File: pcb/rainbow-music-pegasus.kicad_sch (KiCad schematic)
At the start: 83 parts, among them J1 USB_B_Micro, J2 Conn_02x03_Odd_Even, SW1 SW_SPDT, U1 ESP32-C3-MINI-1, U2 OPA344NA, U3 TLV75533PDBV

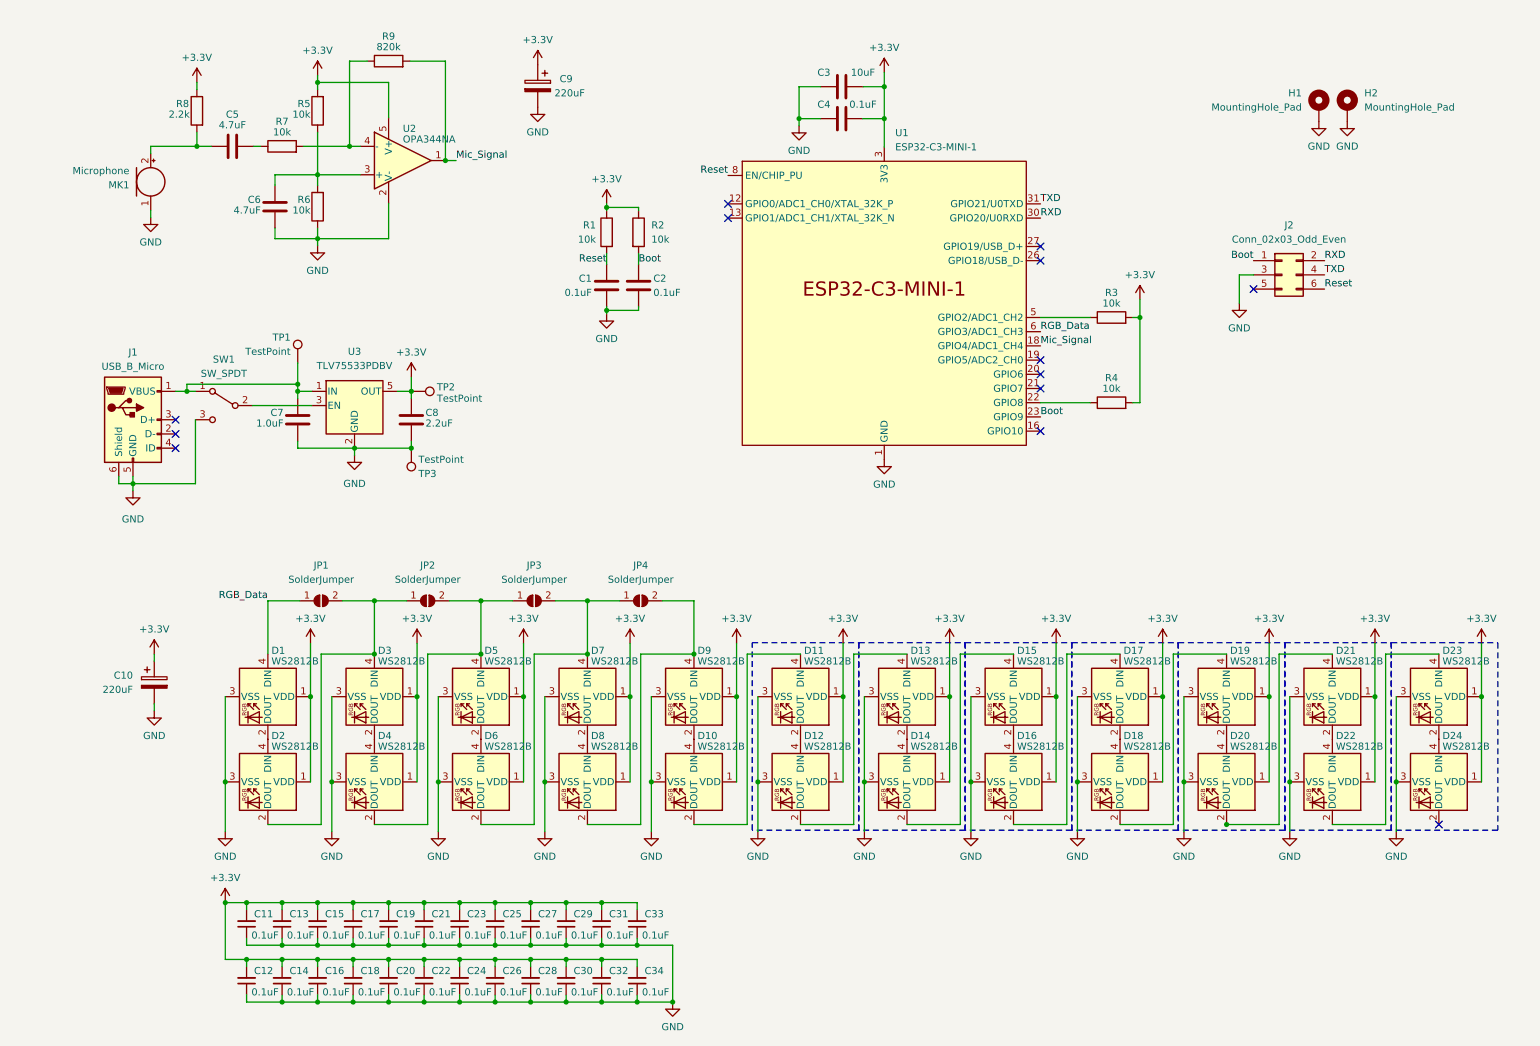
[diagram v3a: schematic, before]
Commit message: Added Altivo cartoon to silkscreen, jumpers for configuring total LEDs installed
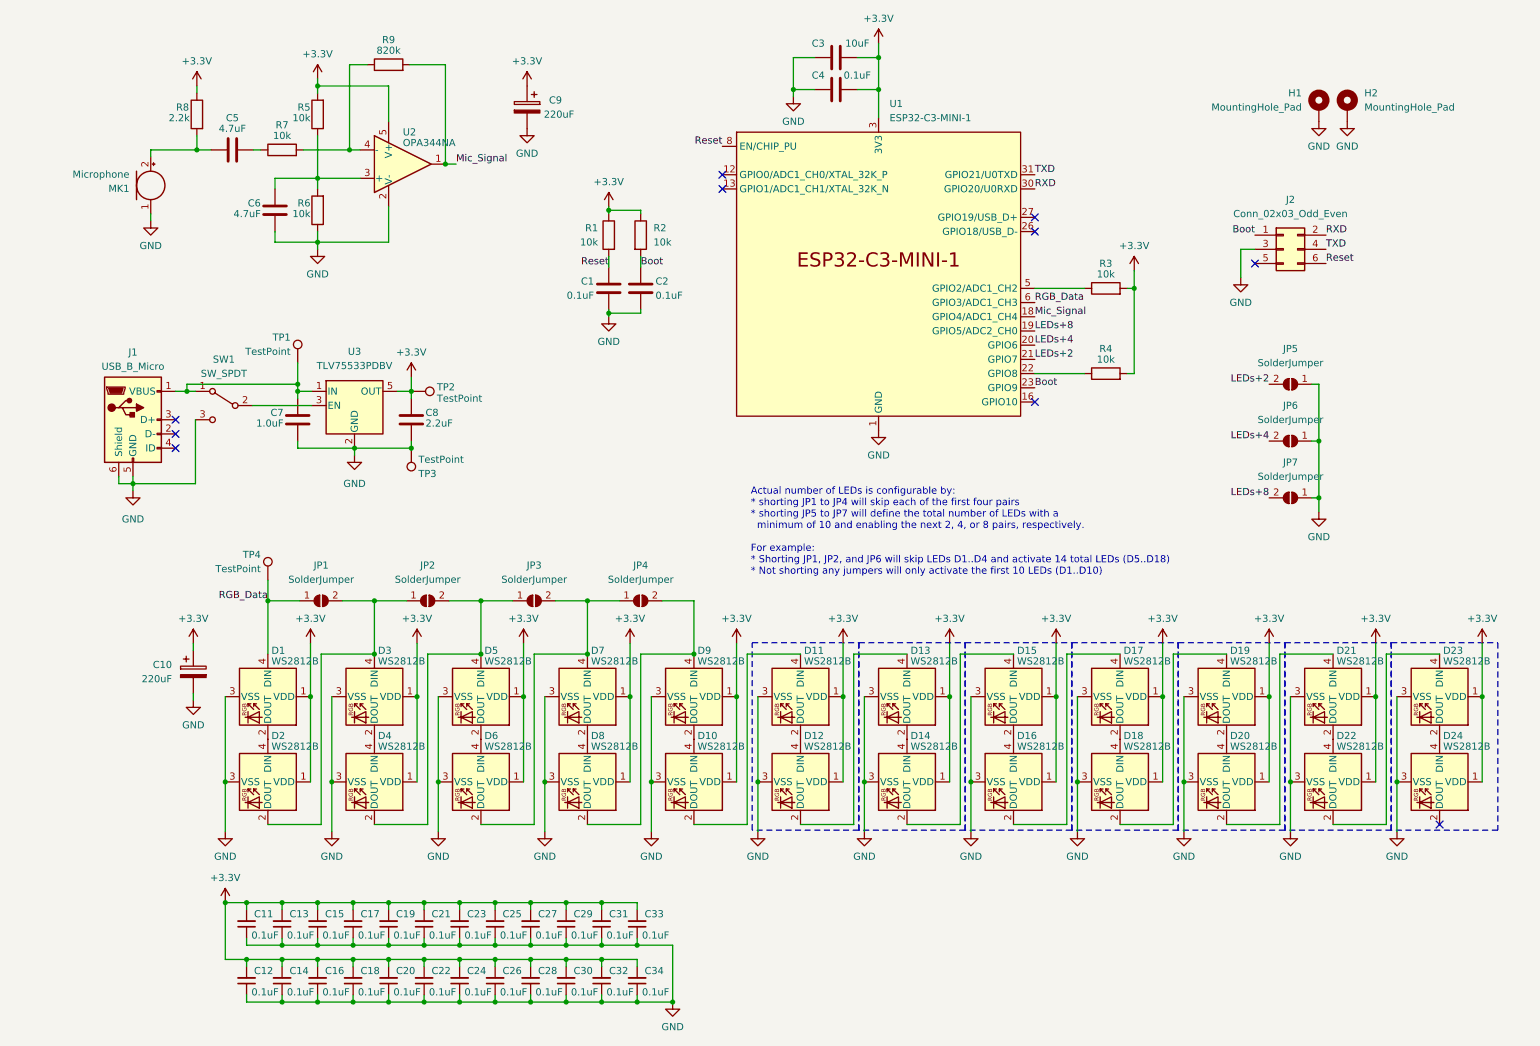
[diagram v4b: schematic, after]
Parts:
- added JP5, JP6, JP7: SolderJumper, Jumper:SolderJumper-2_P1.3mm_Open_TrianglePad1.0x1.5mm, symbol Jumper:SolderJumper_2_Open
- added TP4: TestPoint, TestPoint:TestPoint_THTPad_1.5x1.5mm_Drill0.7mm, symbol Connector:TestPoint
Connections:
- net GND: now also JP5.1 (A), JP6.1 (A), JP7.1 (A)
- net RGB_Data: now also TP4.1
- net LEDs+8: now reaches U1.19 (GPIO5/ADC2_CH0)
- net LEDs+8: now also JP7.2 (B)
- net LEDs+4: now reaches U1.20 (GPIO6)
- net LEDs+4: now also JP6.2 (B)
- net LEDs+2: now reaches U1.21 (GPIO7)
- net LEDs+2: now also JP5.2 (B)
- no-connect marks 13 -> 10
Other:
- note added: "Actual number of LEDs is configurable by: * shorting JP1 to JP4 will skip each of the first four pairs * shorting JP5 to JP7 will define the total number of LEDs with a minimum of 10 and enabling the next 2, 4, or 8 pairs, respectively. For example: * Shorting JP1, JP2, and JP6 will skip LEDs D1..D4 and activate 14 total LEDs (D5..D18) * Not shorting any jumpers will only activate the first 10 LE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"
- moved on the sheet: C1, C10, C2, C3, C4, C5, C6, C9, J2, MK1, R1, R2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

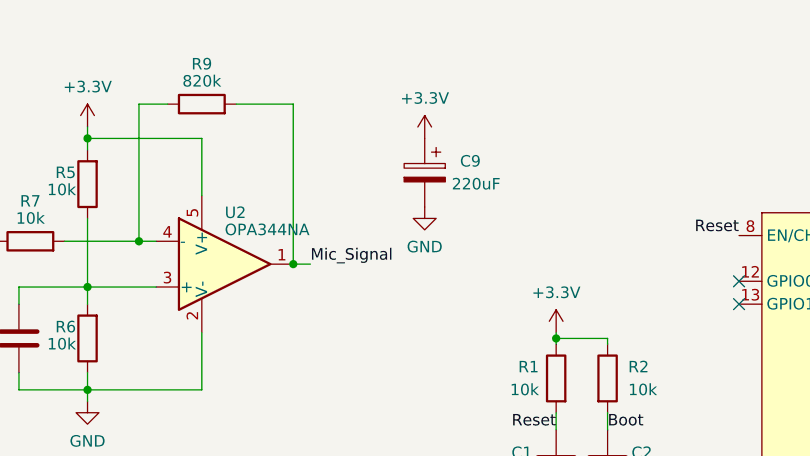
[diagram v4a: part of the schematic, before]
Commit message: Missed a decoupling capacitor at U2; added as C35
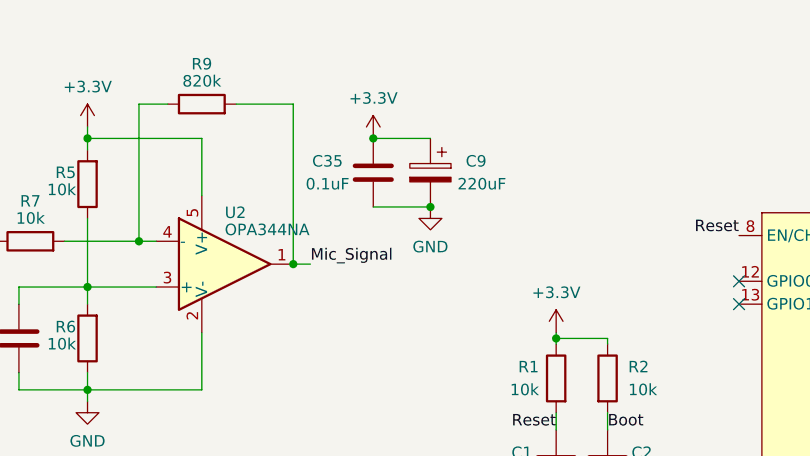
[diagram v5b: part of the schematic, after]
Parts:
- added C35: 0.1uF, Capacitor_SMD:C_0603_1608Metric, symbol Device:C
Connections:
- net +3.3V: now also C35.2
- net GND: now also C35.1
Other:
- moved on the sheet: C9
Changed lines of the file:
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@@
   (junction (at 119.38 180.34) (diameter 0) (color 0 0 0 0)
   )
+  (junction (at 106.68 34.29) (diameter 0) (color 0 0 0 0)
+  )
   (junction (at 74.93 190.5) (diameter 0) (color 0 0 0 0)
   )
@@
   (junction (at 97.79 118.745) (diameter 0) (color 0 0 0 0)
   )
+  (junction (at 100.33 26.67) (diameter 0) (color 0 0 0 0)
+  )
   (junction (at 223.52 151.13) (diameter 0) (color 0 0 0 0)
   )
@@
     (stroke (width 0) (type default))
   )
+  (wire (pts (xy 100.33 34.29) (xy 106.68 34.29))
+    (stroke (width 0) (type default))
+  )
   (wire (pts (xy 81.28 26.67) (xy 81.28 33.02))
     (stroke (width 0) (type default))
@@
     (stroke (width 0) (type default))
   )
+  (wire (pts (xy 100.33 26.67) (xy 106.68 26.67))
+    (stroke (width 0) (type default))
+  )
   (wire (pts (xy 86.36 135.89) (xy 86.36 151.13))
     (stroke (width 0) (type default))
@@
     )
   )
-  (symbol (lib_id "power:GND") (at 106.045 34.29 0) (unit 1)
+  (symbol (lib_id "power:GND") (at 106.68 34.29 0) (unit 1)
     (in_bom yes) (on_board yes) (dnp no) (fields_autoplaced)
-    (property "Reference" "#PWR011" (at 106.045 40.64 0)
+    (property "Reference" "#PWR011" (at 106.68 40.64 0)
       (effects (font (size 1.27 1.27)) hide)
     )
-    (property "Value" "GND" (at 106.045 38.735 0)
+    (property "Value" "GND" (at 106.68 38.735 0)
       (effects (font (size 1.27 1.27)))
     )
-    (property "Footprint" "" (at 106.045 34.29 0)
+    (property "Footprint" "" (at 106.68 34.29 0)
       (effects (font (size 1.27 1.27)) hide)
     )
-    (property "Datasheet" "" (at 106.045 34.29 0)
+    (property "Datasheet" "" (at 106.68 34.29 0)
       (effects (font (size 1.27 1.27)) hide)
     )
@@
     )
   )
-  (symbol (lib_id "power:+3.3V") (at 106.045 26.67 0) (unit 1)
+  (symbol (lib_id "power:+3.3V") (at 100.33 26.67 0) (unit 1)
     (in_bom yes) (on_board yes) (dnp no) (fields_autoplaced)
-    (property "Reference" "#PWR046" (at 106.045 30.48 0)
+    (property "Reference" "#PWR046" (at 100.33 30.48 0)
       (effects (font (size 1.27 1.27)) hide)
     )
-    (property "Value" "+3.3V" (at 106.045 22.225 0)
+    (property "Value" "+3.3V" (at 100.33 22.225 0)
       (effects (font (size 1.27 1.27)))
     )
-    (property "Footprint" "" (at 106.045 26.67 0)
+    (property "Footprint" "" (at 100.33 26.67 0)
       (effects (font (size 1.27 1.27)) hide)
     )
-    (property "Datasheet" "" (at 106.045 26.67 0)
+    (property "Datasheet" "" (at 100.33 26.67 0)
       (effects (font (size 1.27 1.27)) hide)
     )
@@
     )
   )
-  (symbol (lib_id "Device:C_Polarized") (at 106.045 30.48 0) (mirror y) (unit 1)
+  (symbol (lib_id "Device:C_Polarized") (at 106.68 30.48 0) (mirror y) (unit 1)
     (in_bom yes) (on_board yes) (dnp no)
-    (property "Reference" "C9" (at 111.125 29.21 0)
+    (property "Reference" "C9" (at 111.76 29.21 0)
       (effects (font (size 1.27 1.27)))
     )
-    (property "Value" "220uF" (at 111.76 31.75 0)
+    (property "Value" "220uF" (at 112.395 31.75 0)
       (effects (font (size 1.27 1.27)))
     )
-    (property "Footprint" "Capacitor_SMD:CP_Elec_5x5.9" (at 105.0798 34.29 0)
+    (property "Footprint" "Capacitor_SMD:CP_Elec_5x5.9" (at 105.7148 34.29 0)
       (effects (font (size 1.27 1.27)) hide)
     )
-    (property "Datasheet" "~" (at 106.045 30.48 0)
+    (property "Datasheet" "~" (at 106.68 30.48 0)
       (effects (font (size 1.27 1.27)) hide)
     )
@@
         )
       )
+    )
+  )
+  (symbol (lib_id "Device:C") (at 100.33 30.48 180) (unit 1)
+    (in_bom yes) (on_board yes) (dnp no)
+    (property "Reference" "C35" (at 95.25 29.21 0)
+      (effects (font (size 1.27 1.27)))
+    )
+    (property "Value" "0.1uF" (at 95.25 31.75 0)
+      (effects (font (size 1.27 1.27)))
+    )
+    (property "Footprint" "Capacitor_SMD:C_0603_1608Metric" (at 99.3648 26.67 0)
+      (effects (font (size 1.27 1.27)) hide)
+    )
+    (property "Datasheet" "~" (at 100.33 30.48 0)
+      (effects (font (size 1.27 1.27)) hide)
+    )
+    (pin "1")
+    (pin "2")
+    (instances
+      (project "rainbow-music-pegasus"
+        (path "/4cbaa20b-39f5-487e-a5d4-6b04539cf52b"
+          (reference "C35") (unit 1)
+        )
+      )

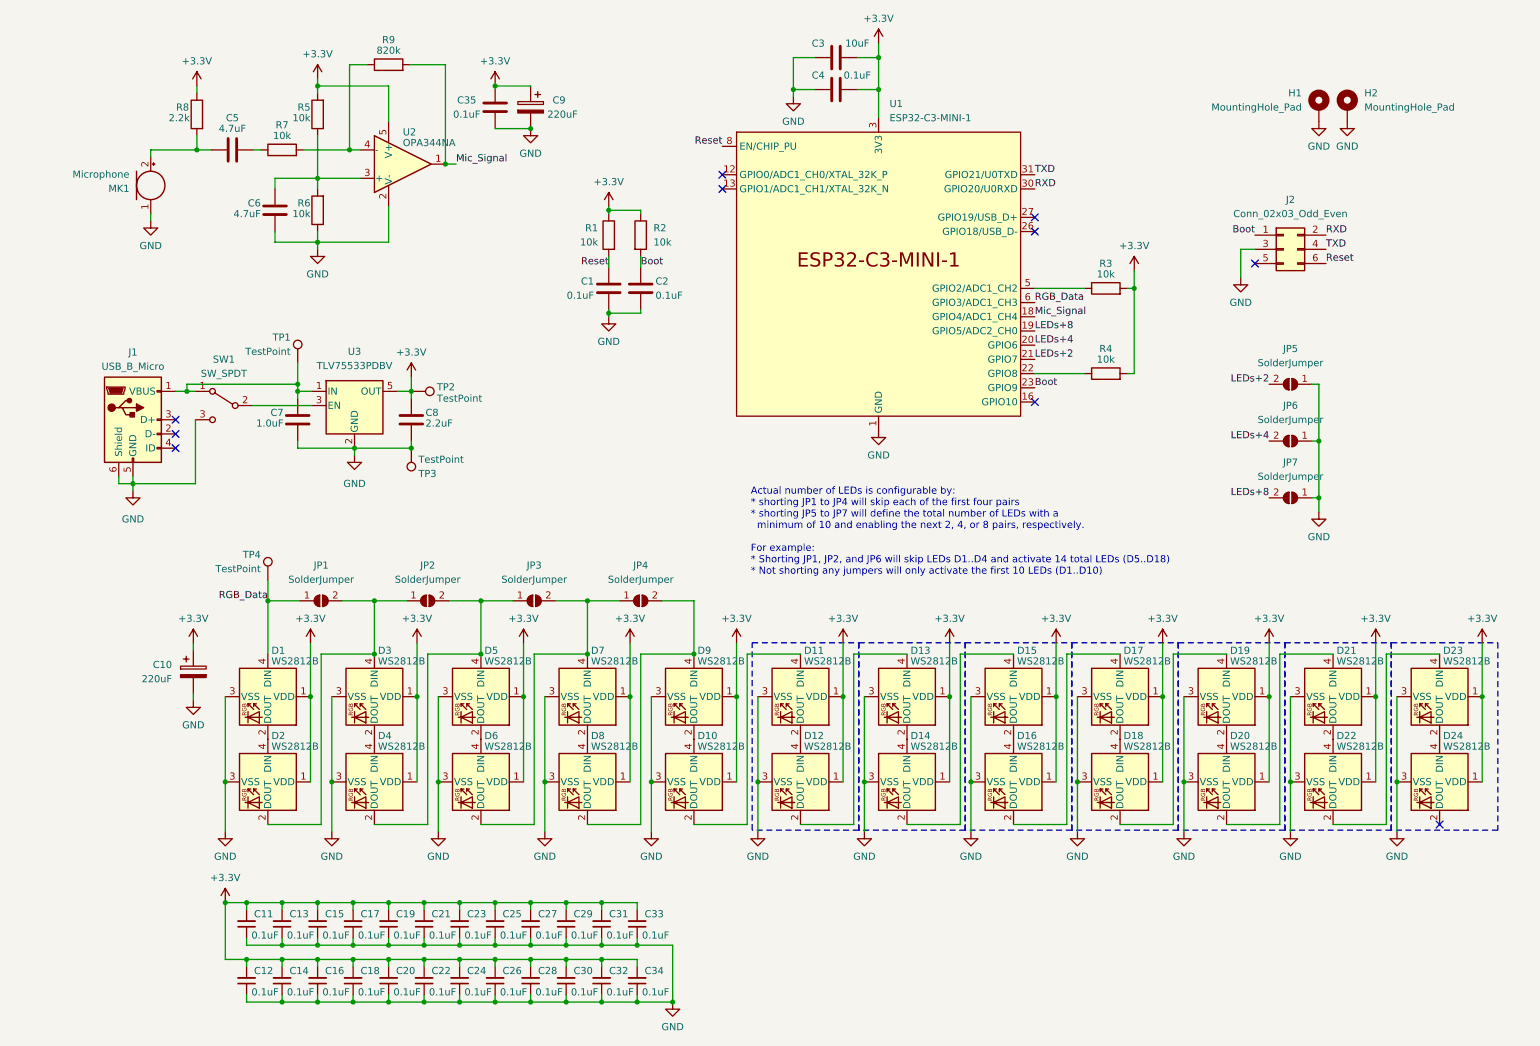
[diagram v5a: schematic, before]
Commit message: Snapshots of ths BOM, Schematics; added license and readme starter.
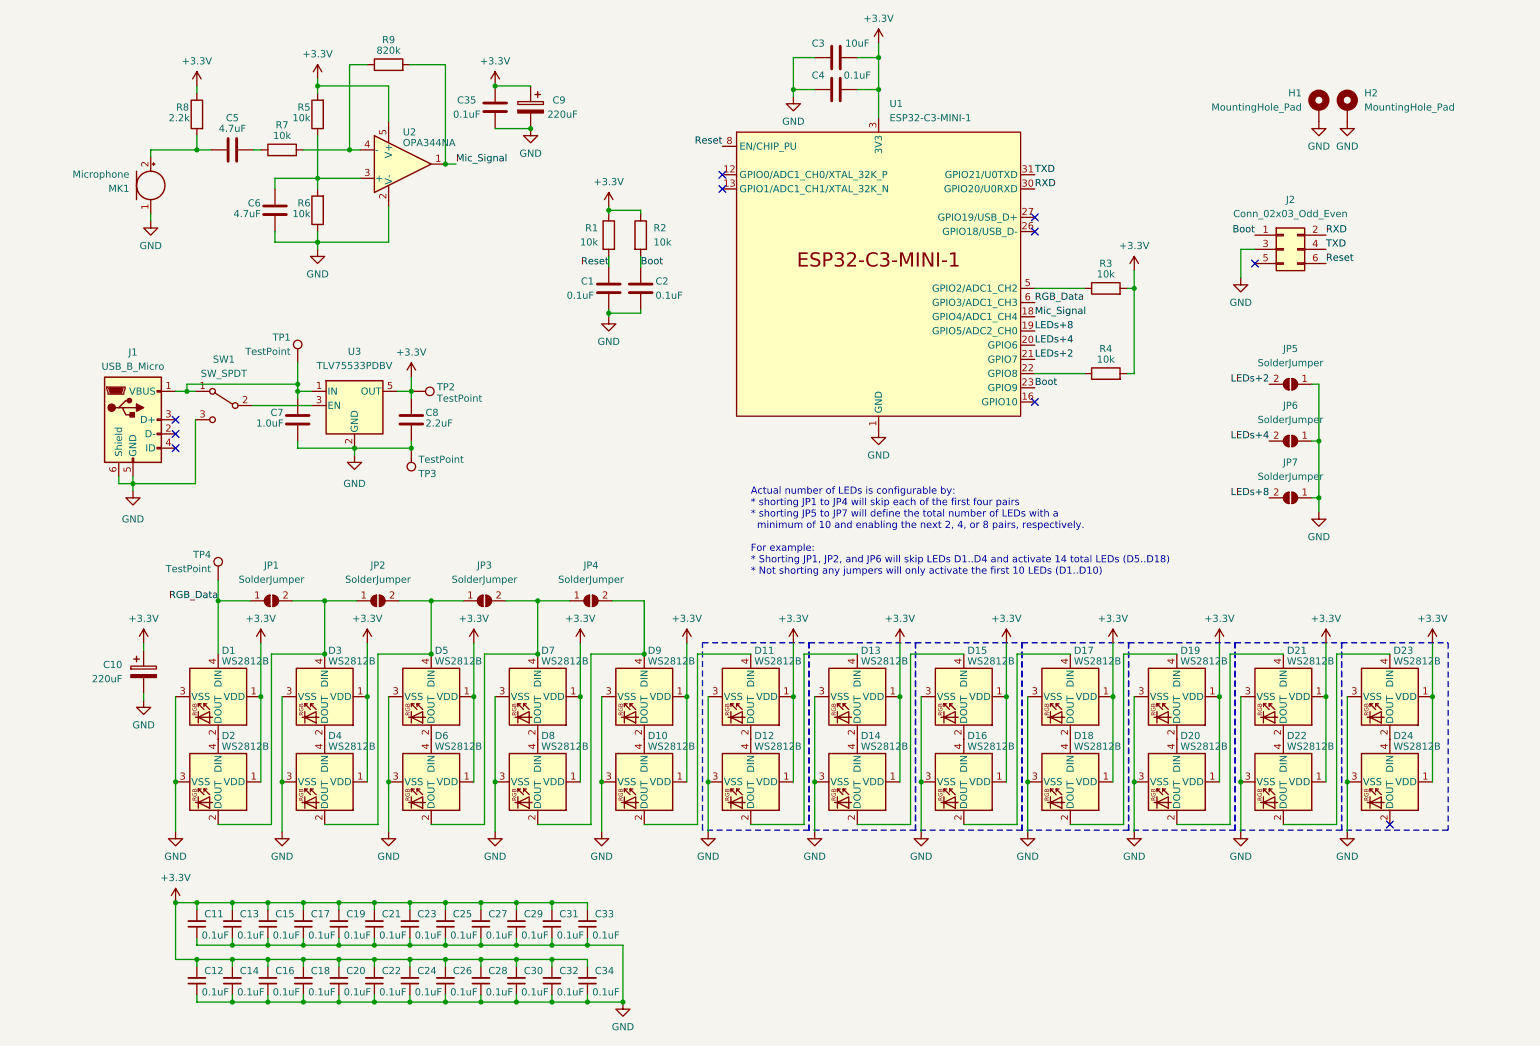
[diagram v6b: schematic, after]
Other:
- moved on the sheet: C10, C11, C12, C13, C14, C15, C16, C17, C18, C19, C20, C21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
